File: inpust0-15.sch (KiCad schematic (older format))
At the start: 160 parts

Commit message: finished resistors0-31
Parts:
- R0_0, R0_2, R0_3, R0_5, R0_6, R0_8, R10_0, R10_3, R10_4, R10_5, R10_6, R10_7, R10_8, R10_9, R11_0, R11_1, R11_2, R11_4, R11_7, R11_9, R12_2, R12_3, R12_5, R12_6, R12_7, R12_9, R13_1, R13_2, R13_4, R13_5, R13_7, R14_0, R14_1, R14_3, R14_5, R14_6, R14_8, R14_9, R15_0, R15_2, R15_5, R15_7, R15_8, R15_9, R1_1, R1_2, R1_3, R1_4, R1_5, R1_6, R2_0, R2_1, R2_2, R2_3, R2_5, R2_6, R2_8, R3_0, R3_1, R3_4, R3_5, R3_6, R3_7, R3_9, R4_0, R4_1, R4_2, R4_4, R4_6, R4_8, R4_9, R5_0, R5_1, R5_2, R5_4, R5_5, R5_6, R5_7, R6_0, R6_1, R6_5, R6_6, R6_8, R7_1, R7_2, R7_3, R7_4, R7_5, R7_6, R7_8, R8_0, R8_2, R8_3, R8_5, R8_6, R8_8, R8_9, R9_1, R9_3, R9_4, R9_5, R9_7, R9_8, R9_9: value 999 -> 9999

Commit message: Added footprints, finished schematic, began PCB layout
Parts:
- R0_0, R0_1, R0_2, R0_3, R0_4, R0_5, R0_6, R0_7, R0_8, R0_9, R10_0, R10_1, R10_2, R10_3, R10_4, R10_5, R10_6, R10_7, R10_8, R10_9, R11_0, R11_1, R11_2, R11_3, R11_4, R11_5, R11_6, R11_7, R11_8, R11_9, R12_0, R12_1, R12_2, R12_3, R12_4, R12_5, R12_6, R12_7, R12_8, R12_9, R13_0, R13_1, R13_2, R13_3, R13_4, R13_5, R13_6, R13_7, R13_8, R13_9, R14_0, R14_1, R14_2, R14_3, R14_4, R14_5, R14_6, R14_7, R14_8, R14_9, R15_0, R15_1, R15_2, R15_3, R15_4, R15_5, R15_6, R15_7, R15_8, R15_9, R1_0, R1_1, R1_2, R1_3, R1_4, R1_5, R1_6, R1_7, R1_8, R1_9, R2_0, R2_1, R2_2, R2_3, R2_4, R2_5, R2_6, R2_7, R2_8, R2_9, R3_0, R3_1, R3_2, R3_3, R3_4, R3_5, R3_6, R3_7, R3_8, R3_9, R4_0, R4_1, R4_2, R4_3, R4_4, R4_5, R4_6, R4_7, R4_8, R4_9, R5_0, R5_1, R5_2, R5_3, R5_4, R5_5, R5_6, R5_7, R5_8, R5_9, R6_0, R6_1, R6_2, R6_3, R6_4, R6_5, R6_6, R6_7, R6_8, R6_9, R7_0, R7_1, R7_2, R7_3, R7_4, R7_5, R7_6, R7_7, R7_8, R7_9, R8_0, R8_1, R8_2, R8_3, R8_4, R8_5, R8_6, R8_7, R8_8, R8_9, R9_0, R9_1, R9_2, R9_3, R9_4, R9_5, R9_6, R9_7, R9_8, R9_9: footprint (none) -> Resistors_SMD:R_1206

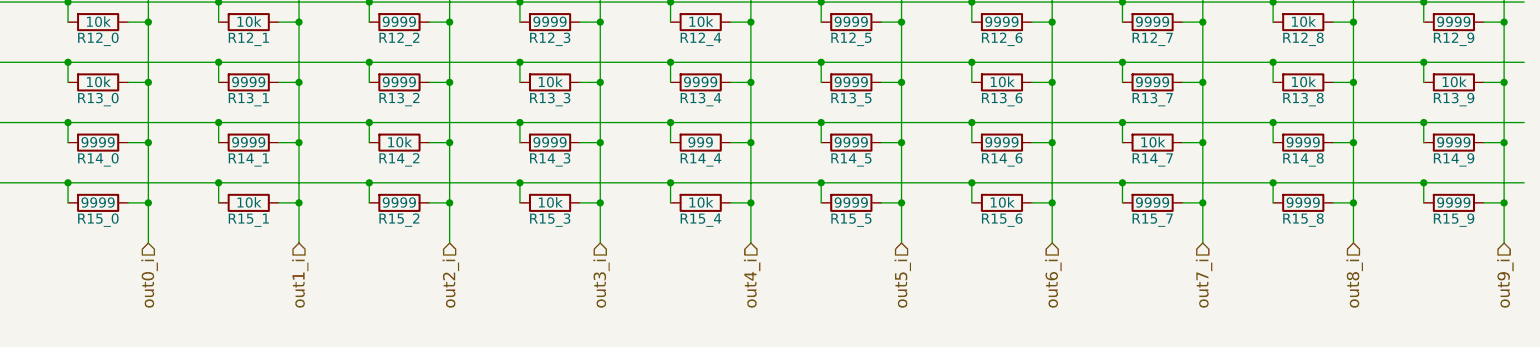
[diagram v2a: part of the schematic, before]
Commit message: fixed resistor schematic errors
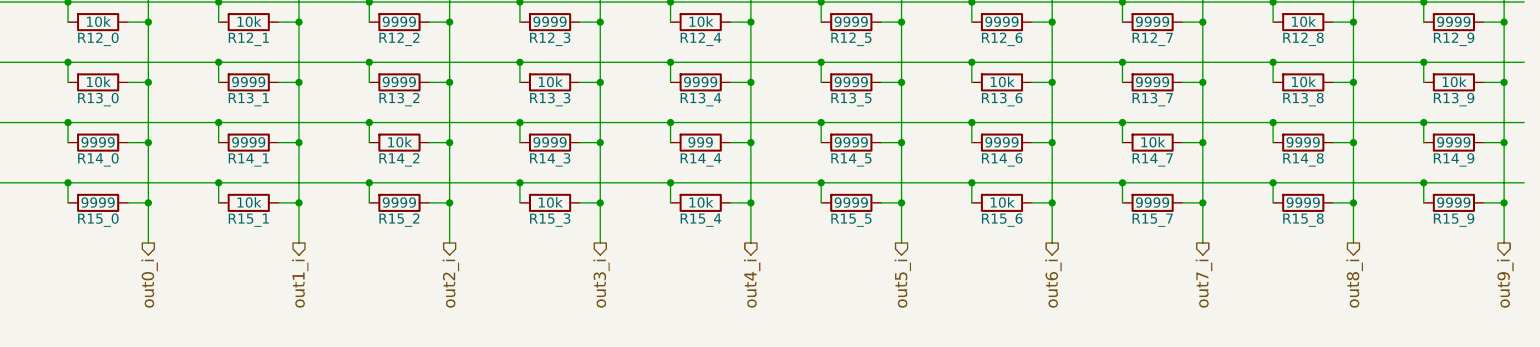
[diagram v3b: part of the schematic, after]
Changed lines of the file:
@@
 Text HLabel 2200 5800 0    60   Input ~ 0
 in15_v
-Text HLabel 3050 6100 3    60   Input ~ 0
+Text HLabel 3050 6100 3    60   Output ~ 0
 out0_i
-Text HLabel 3800 6100 3    60   Input ~ 0
+Text HLabel 3800 6100 3    60   Output ~ 0
 out1_i
-Text HLabel 4550 6100 3    60   Input ~ 0
+Text HLabel 4550 6100 3    60   Output ~ 0
 out2_i
-Text HLabel 5300 6100 3    60   Input ~ 0
+Text HLabel 5300 6100 3    60   Output ~ 0
 out3_i
-Text HLabel 6050 6100 3    60   Input ~ 0
+Text HLabel 6050 6100 3    60   Output ~ 0
 out4_i
-Text HLabel 6800 6100 3    60   Input ~ 0
+Text HLabel 6800 6100 3    60   Output ~ 0
 out5_i
-Text HLabel 7550 6100 3    60   Input ~ 0
+Text HLabel 7550 6100 3    60   Output ~ 0
 out6_i
-Text HLabel 8300 6100 3    60   Input ~ 0
+Text HLabel 8300 6100 3    60   Output ~ 0
 out7_i
-Text HLabel 9050 6100 3    60   Input ~ 0
+Text HLabel 9050 6100 3    60   Output ~ 0
 out8_i
-Text HLabel 9800 6100 3    60   Input ~ 0
+Text HLabel 9800 6100 3    60   Output ~ 0
 out9_i
 $Comp
